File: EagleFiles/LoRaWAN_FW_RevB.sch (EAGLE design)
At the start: 13 parts

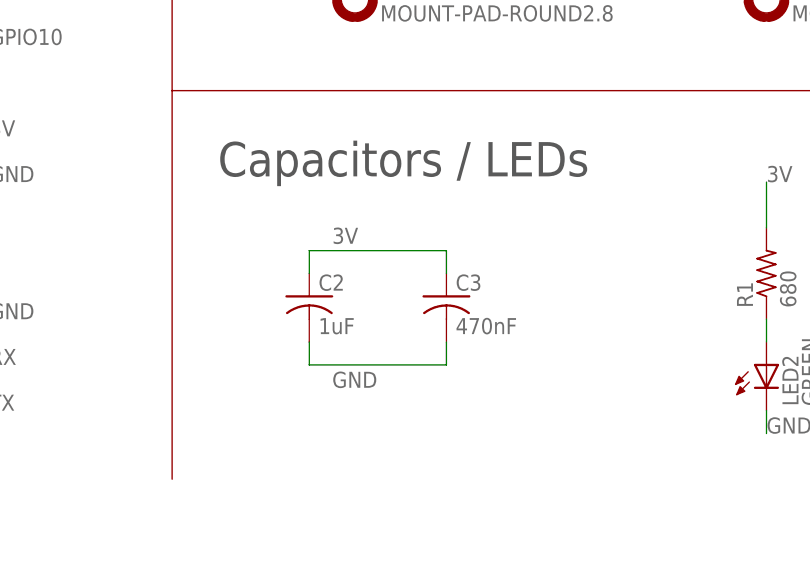
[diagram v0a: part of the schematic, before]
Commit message: Updated Eagle files
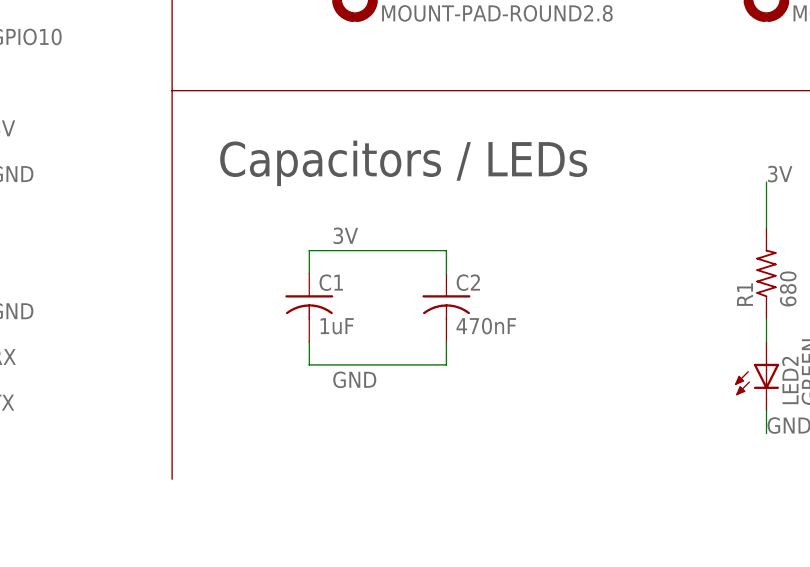
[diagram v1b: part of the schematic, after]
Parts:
- removed C3: 470nF, adafruit:C-USC0603
- added C1: 1uF, adafruit:C-USC0603
- C2: value 1uF -> 470nF
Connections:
- net 3V: now also C1.1; no longer C3.1
- net GND: now also C1.2; no longer C3.2
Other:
- moved on the sheet: C2
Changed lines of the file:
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@@
 </classes>
 <parts>
-<part name="C3" library="adafruit" deviceset="C-US" device="C0603" value="470nF"/>
+<part name="C2" library="adafruit" deviceset="C-US" device="C0603" value="470nF"/>
 <part name="LED2" library="adafruit" deviceset="LED" device="CHIPLED_0805" value="GREEN"/>
 <part name="R1" library="adafruit2" deviceset="R-US_" device="R0603" value="680"/>
@@
 <part name="H2" library="holes" deviceset="MOUNT-PAD-ROUND" device="2.8"/>
 <part name="FRAME2" library="frames" deviceset="FRAME_A_L" device=""/>
-<part name="C2" library="adafruit" deviceset="C-US" device="C0603" value="1uF"/>
+<part name="C1" library="adafruit" deviceset="C-US" device="C0603" value="1uF"/>
 <part name="X1" library="adafruit" deviceset="SMACONNECTOR" device="_EDGE"/>
 <part name="U1" library="SyncChannelCustom" deviceset="RN2483/RN2903" device=""/>
@@
 </plain>
 <instances>
-<instance part="C3" gate="G$1" x="203.2" y="55.88"/>
+<instance part="C2" gate="G$1" x="203.2" y="55.88"/>
 <instance part="LED2" gate="G$1" x="238.76" y="48.26"/>
 <instance part="R1" gate="G$1" x="238.76" y="58.42" rot="R90"/>
@@
 <instance part="H2" gate="G$1" x="238.76" y="88.9"/>
 <instance part="FRAME2" gate="G$2" x="172.72" y="0"/>
-<instance part="C2" gate="G$1" x="187.96" y="55.88"/>
+<instance part="C1" gate="G$1" x="187.96" y="55.88"/>
 <instance part="X1" gate="G$1" x="119.38" y="142.24" rot="R90"/>
 <instance part="U1" gate="U$1" x="114.3" y="50.8"/>
@@
 <label x="190.5" y="45.72" size="1.778" layer="95"/>
 <wire x1="203.2" y1="48.26" x2="187.96" y2="48.26" width="0.1524" layer="91"/>
+<pinref part="C1" gate="G$1" pin="2"/>
 <pinref part="C2" gate="G$1" pin="2"/>
-<pinref part="C3" gate="G$1" pin="2"/>
 <wire x1="203.2" y1="50.8" x2="203.2" y2="48.26" width="0.1524" layer="91"/>
 </segment>
@@
 <label x="190.5" y="61.722" size="1.778" layer="95"/>
 <wire x1="203.2" y1="60.96" x2="187.96" y2="60.96" width="0.1524" layer="91"/>
+<pinref part="C1" gate="G$1" pin="1"/>
 <pinref part="C2" gate="G$1" pin="1"/>
-<pinref part="C3" gate="G$1" pin="1"/>
 <wire x1="203.2" y1="58.42" x2="203.2" y2="60.96" width="0.1524" layer="91"/>
 </segment>
